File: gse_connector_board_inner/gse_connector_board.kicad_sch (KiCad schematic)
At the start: 26 parts, among them J1 arming_connector, J2 gse_com_connector, J3 chg_connector, J4 Conn_02x03_Top_Bottom, J5 Conn_02x02_Top_Bottom, U7 ISO1044BD, U9 MCP2562-E-SN

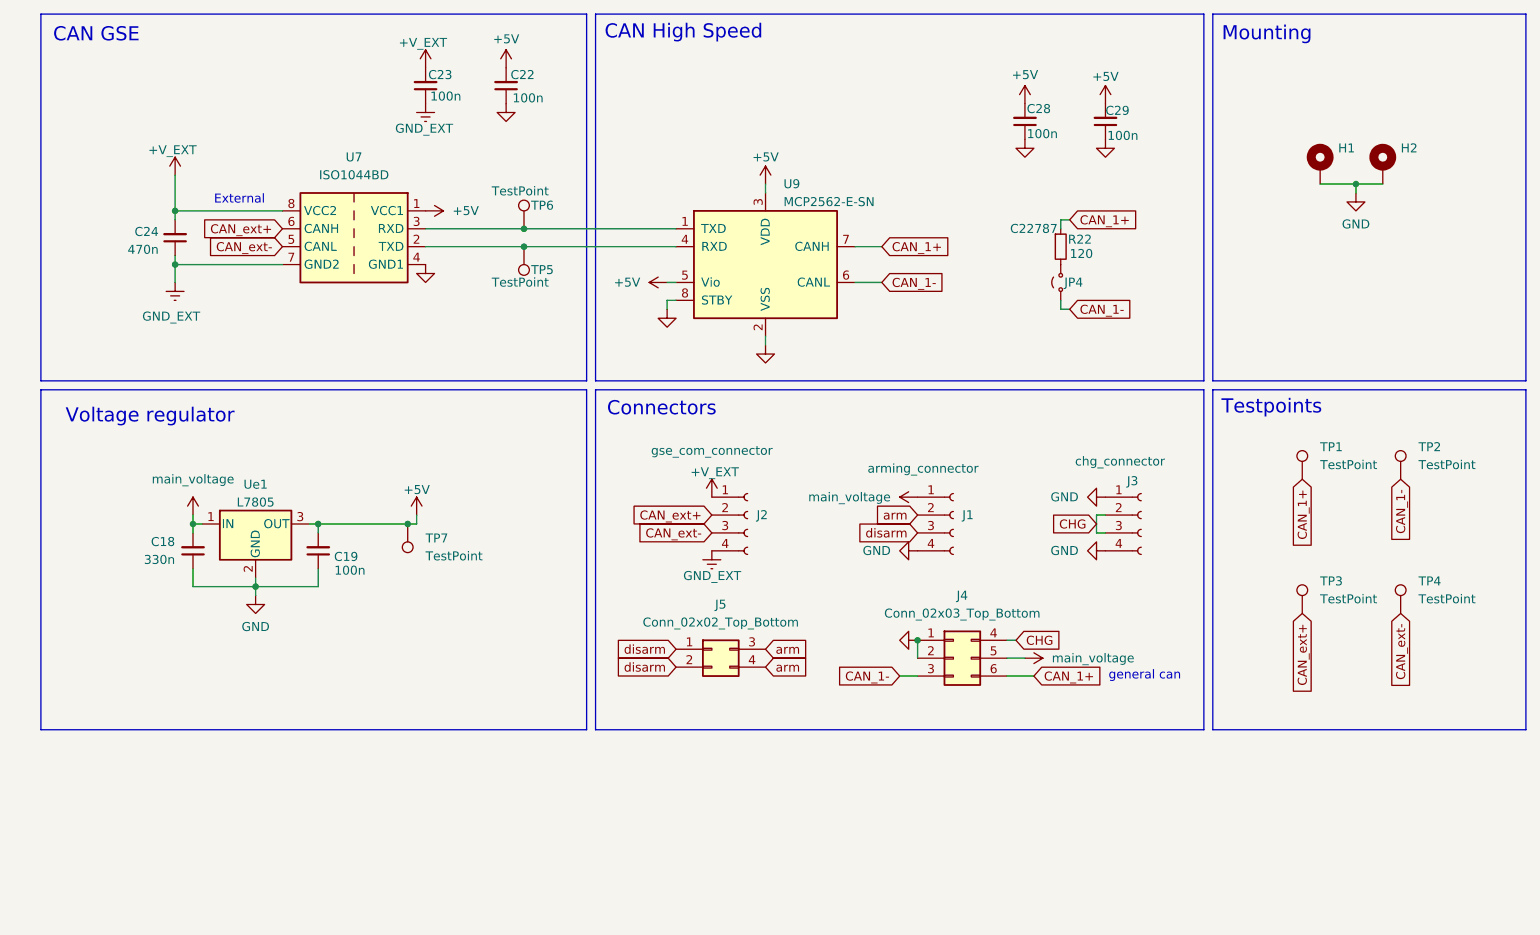
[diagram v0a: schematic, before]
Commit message: changed the footprints of the magnetic connector and routing of inner board
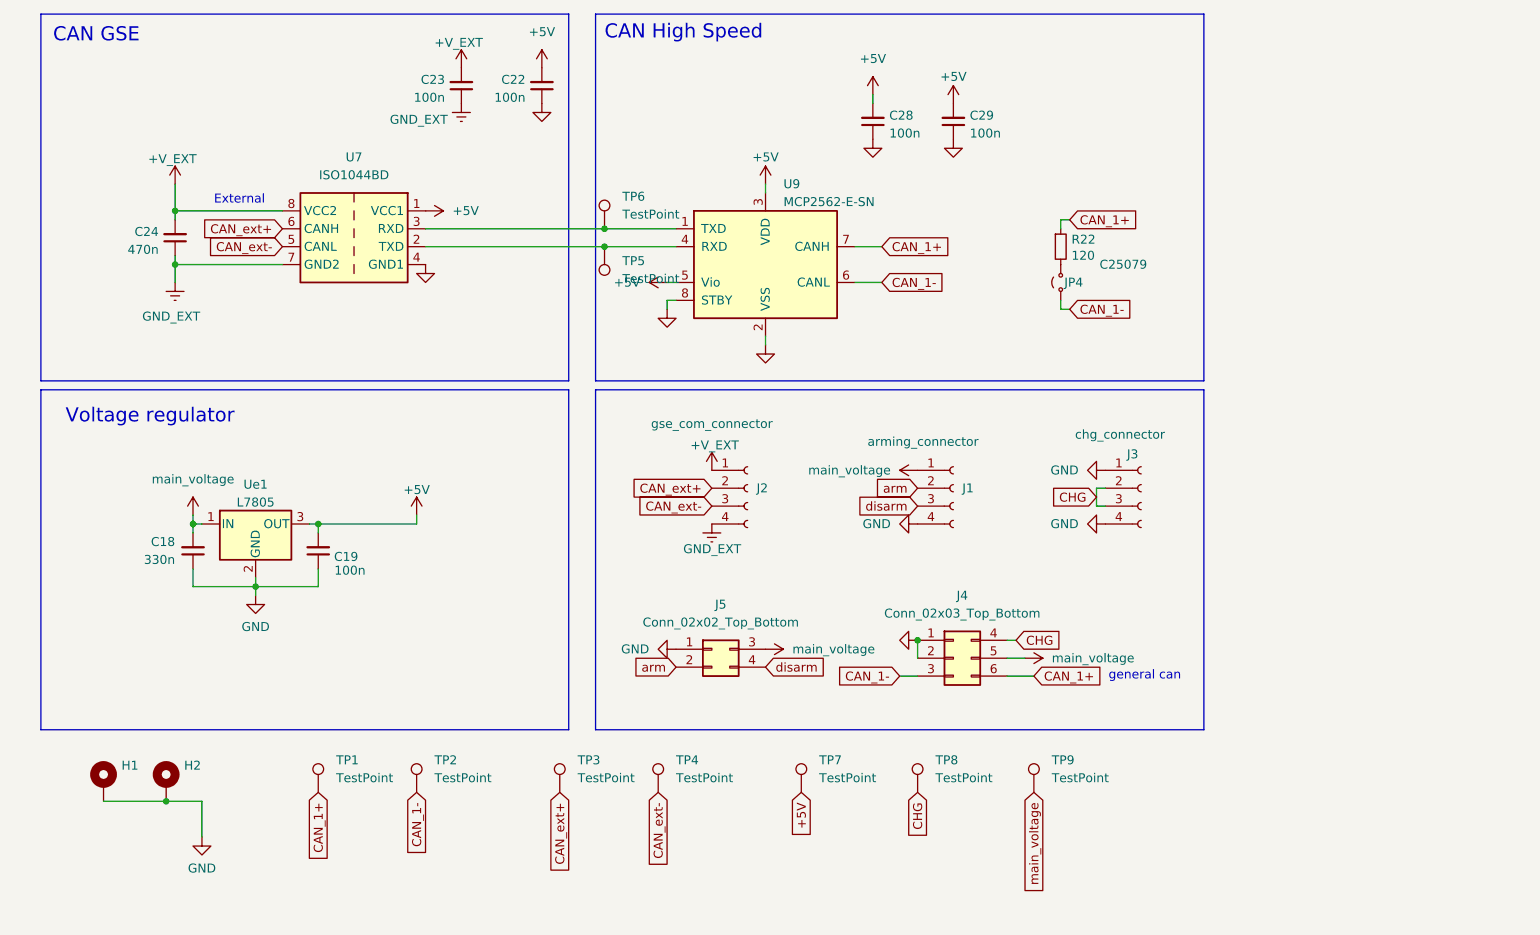
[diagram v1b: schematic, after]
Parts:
- added TP8, TP9: TestPoint, TestPoint:TestPoint_Pad_1.0x1.0mm, symbol Connector:TestPoint
- C18, C19: footprint Capacitor_SMD:C_0603_1608Metric_Pad1.08x0.95mm_HandSolder -> Capacitor_SMD:C_0603_1608Metric
- R22: footprint Resistor_SMD:R_0603_1608Metric_Pad0.98x0.95mm_HandSolder -> Resistor_SMD:R_0402_1005Metric; LCSC C22787 -> C25079; Part# (none) -> RC0603FR-07120RL
- TP1, TP2, TP3, TP4, TP5, TP6, TP7: footprint TestPoint:TestPoint_Pad_D1.0mm -> TestPoint:TestPoint_Pad_1.0x1.0mm
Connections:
- net CHG: now also TP8.1
- net GND: now also J5.1 (Pin_1)
- net arm: now also J5.2 (Pin_2); no longer J5.3 (Pin_3), J5.4 (Pin_4)
- net disarm: now also J5.4 (Pin_4); no longer J5.1 (Pin_1), J5.2 (Pin_2)
- net main_voltage: now also J5.3 (Pin_3), TP9.1
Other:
- note removed: "Connectors"
- note removed: "Mounting"
- note removed: "Testpoints"
- company: TUDSaT -> (none)
- title: GSE connector board (inner) -> (none)
- moved on the sheet: C22, C23, C28, C29, J1, J2, J3, TP5, TP6

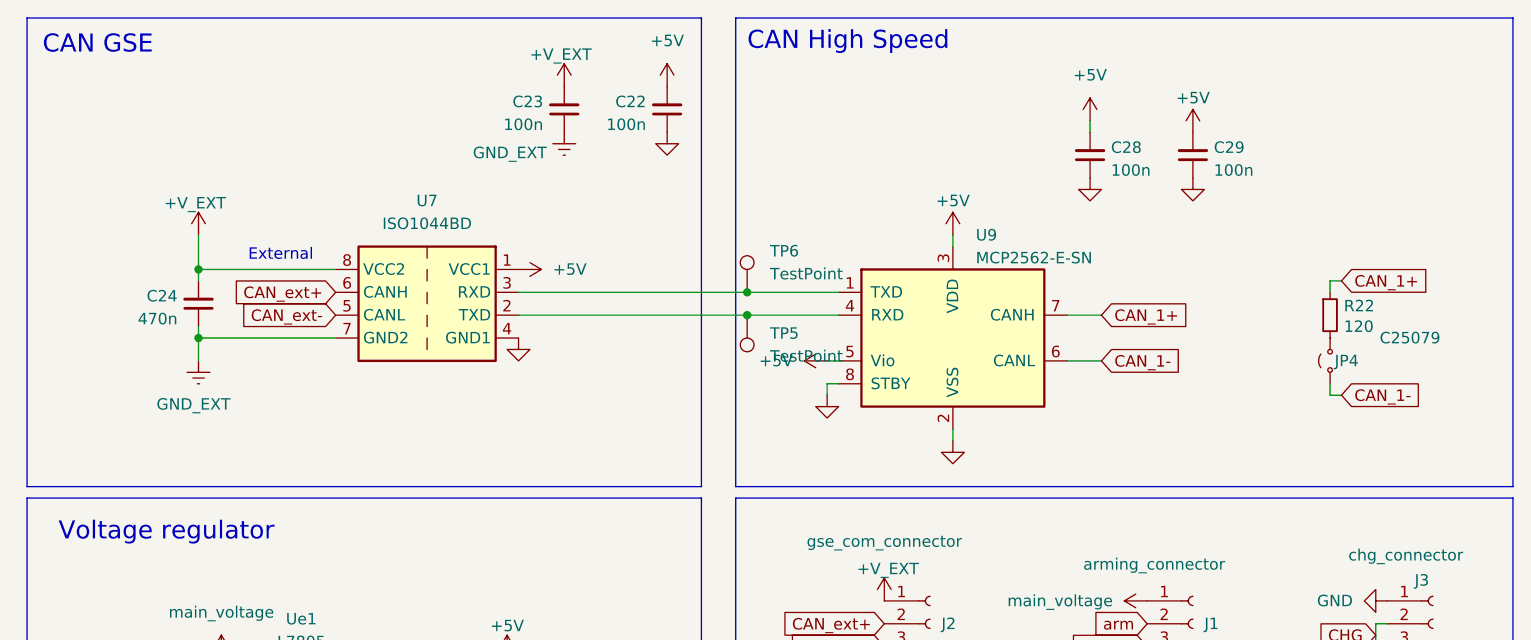
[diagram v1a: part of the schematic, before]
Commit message: adapted footprints, scematics and routing
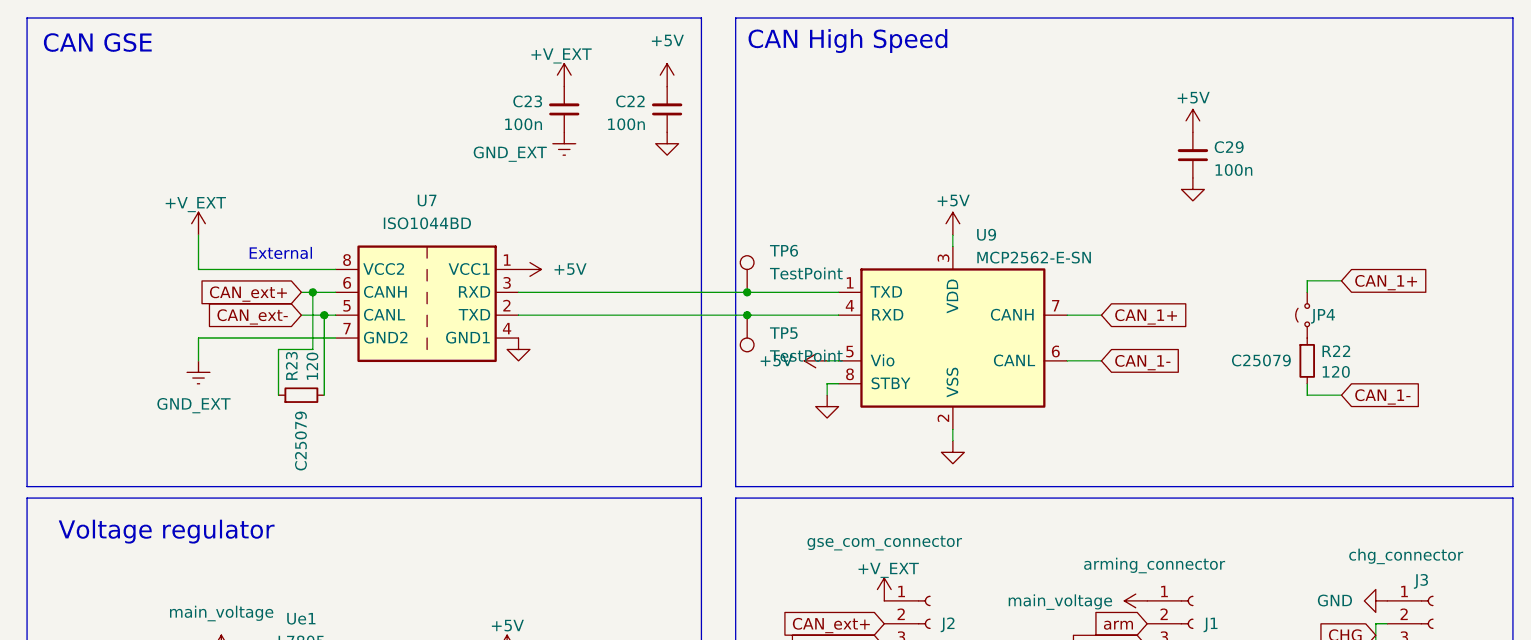
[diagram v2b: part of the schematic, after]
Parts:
- removed C24: 470n, Capacitor_SMD:C_0603_1608Metric_Pad1.08x0.95mm_HandSolder, symbol Device:C_Small
- removed C28: 100n, Capacitor_SMD:C_0603_1608Metric_Pad1.08x0.95mm_HandSolder, symbol Device:C_Small
- added R23: 120, Resistor_SMD:R_0402_1005Metric, symbol Device:R_Small
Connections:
- net CAN_1+: now also JP4.2 (B); no longer R22.1
- net CAN_1-: now also R22.2; no longer JP4.1 (A)
- net CAN_ext+: now also R23.1
- net CAN_ext-: now also R23.2
- new net: JP4.1 (A), R22.1
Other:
- moved on the sheet: JP4, R22

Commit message: implemented changes
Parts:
- J1, J2, J3: footprint custom_parts:4_pin_mag_con_new -> custom_parts:4_pin_mag_con_flat; now not fitted
- R23: KiLib_Generator (none) -> SMD_2terminal_chip_molded
- TP1, TP2, TP3, TP4, TP5, TP6, TP7, TP8, TP9: footprint TestPoint:TestPoint_Pad_1.0x1.0mm -> TestPoint:TestPoint_Pad_D1.5mm
- Ue1: LCSC# (none) -> C310413
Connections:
- net GND: no longer J1.4 (Pin_4), J5.1 (Pin_1)
- net main_voltage: no longer J1.1 (Pin_1), J5.3 (Pin_3)
- new net GND_Arm: J1.4 (Pin_4), J5.1 (Pin_1)
- new net voltage_Arm: J1.1 (Pin_1), J5.3 (Pin_3)
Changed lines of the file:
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@@
 			)
 		)
-		(property "Footprint" "TestPoint:TestPoint_Pad_1.0x1.0mm"
+		(property "Footprint" "TestPoint:TestPoint_Pad_D1.5mm"
 			(at 95.25 125.73 0)
 			(hide yes)
@@
 			)
 		)
-		(property "Value" "GND"
+		(property "Value" "GND_Arm"
 			(at 137.16 87.6299 90)
 			(show_name no)
@@
 			)
 		)
-		(property "Footprint" "TestPoint:TestPoint_Pad_1.0x1.0mm"
+		(property "Footprint" "TestPoint:TestPoint_Pad_D1.5mm"
 			(at 74.93 125.73 0)
 			(hide yes)
@@
 		(on_board yes)
 		(in_pos_files yes)
-		(dnp no)
+		(dnp yes)
 		(property "Reference" "J3"
 			(at 170.688 77.724 0)
@@
 			)
 		)
-		(property "Footprint" "custom_parts:4_pin_mag_con_new"
+		(property "Footprint" "custom_parts:4_pin_mag_con_flat"
 			(at 172.72 82.55 0)
 			(hide yes)
@@
 		(on_board yes)
 		(in_pos_files yes)
-		(dnp no)
+		(dnp yes)
 		(property "Reference" "J1"
 			(at 147.32 82.5499 0)
@@
 			)
 		)
-		(property "Footprint" "custom_parts:4_pin_mag_con_new"
+		(property "Footprint" "custom_parts:4_pin_mag_con_flat"
 			(at 146.05 82.55 0)
 			(hide yes)
@@
 			)
 		)
+		(property "LCSC#" "C310413"
+			(at 46.99 87.63 0)
+			(hide yes)
+			(show_name no)
+			(do_not_autoplace no)
+			(effects
+				(font
+					(size 1.27 1.27)
+				)
+			)
+		)
 		(pin "1"
 		)
@@
 			)
 		)
-		(property "Footprint" "TestPoint:TestPoint_Pad_1.0x1.0mm"
+		(property "Footprint" "TestPoint:TestPoint_Pad_D1.5mm"
 			(at 101.6 45.72 0)
 			(hide yes)
@@
 			)
 		)
-		(property "Value" "main_voltage"
+		(property "Value" "voltage_Arm"
 			(at 123.19 105.4099 90)
 			(show_name no)
@@
 			)
 		)
-		(property "Footprint" "TestPoint:TestPoint_Pad_1.0x1.0mm"
+		(property "Footprint" "TestPoint:TestPoint_Pad_D1.5mm"
 			(at 129.54 125.73 0)
 			(hide yes)
@@
 			)
 		)
+		(property "KiLib_Generator" "SMD_2terminal_chip_molded"
+			(at 46.99 57.15 0)
+			(hide yes)
+			(show_name no)
+			(do_not_autoplace no)
+			(effects
+				(font
+					(size 1.27 1.27)
+				)
+			)
+		)
 		(pin "1"
 		)
@@
 			)
 		)
-		(property "Footprint" "TestPoint:TestPoint_Pad_1.0x1.0mm"
+		(property "Footprint" "TestPoint:TestPoint_Pad_D1.5mm"
 			(at 60.96 125.73 0)
 			(hide yes)
@@
 			)
 		)
-		(property "Footprint" "TestPoint:TestPoint_Pad_1.0x1.0mm"
+		(property "Footprint" "TestPoint:TestPoint_Pad_D1.5mm"
 			(at 109.22 125.73 0)
 			(hide yes)
@@
 			)
 		)
-		(property "Footprint" "TestPoint:TestPoint_Pad_1.0x1.0mm"
+		(property "Footprint" "TestPoint:TestPoint_Pad_D1.5mm"
 			(at 162.56 125.73 0)
 			(hide yes)
@@
 			)
 		)
-		(property "Footprint" "TestPoint:TestPoint_Pad_1.0x1.0mm"
+		(property "Footprint" "TestPoint:TestPoint_Pad_D1.5mm"
 			(at 146.05 125.73 0)
 			(hide yes)
@@
 			)
 		)
-		(property "Value" "main_voltage"
+		(property "Value" "voltage_Arm"
 			(at 137.16 80.0099 90)
 			(show_name no)
@@
 			)
 		)
-		(property "Value" "GND"
+		(property "Value" "GND_Arm"
 			(at 102.87 105.4099 90)
 			(show_name no)
@@
 		(on_board yes)
 		(in_pos_files yes)
-		(dnp no)
+		(dnp yes)
 		(property "Reference" "J2"
 			(at 118.11 82.5499 0)
@@
 			)
 		)
-		(property "Footprint" "custom_parts:4_pin_mag_con_new"
+		(property "Footprint" "custom_parts:4_pin_mag_con_flat"
 			(at 116.84 82.55 0)
 			(hide yes)
@@
 			)
 		)
-		(property "Footprint" "TestPoint:TestPoint_Pad_1.0x1.0mm"
+		(property "Footprint" "TestPoint:TestPoint_Pad_D1.5mm"
 			(at 91.44 48.26 0)
 			(hide yes)
